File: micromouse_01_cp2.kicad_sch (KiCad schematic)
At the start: 40 parts, among them IC1 ESP32-S3FH4R2, IC2 MPU-6500, IC3 AS5047P-ATSM, IC4 AS5047P-ATSM, IC5 DRV8835DSSR, J2 USB_B_Micro, M1 MK06-4.5, M2 MK06-4.5, SW2 SW_Push, U7 RTV-104DF333-S-40.000-TR

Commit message: [fix]アンテナ除去
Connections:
- net GND: now also J2.6 (Shield)
- no-connect marks 46 -> 45
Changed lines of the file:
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@@
   (no_connect (at 35.56 40.64))
   (no_connect (at 71.12 106.68))
-  (no_connect (at 38.1 81.28))
   (no_connect (at 104.14 43.18))
   (no_connect (at 134.62 43.18))
@@
     (stroke (width 0) (type default))
   )
+  (wire (pts (xy 38.1 88.9) (xy 40.64 88.9))
+    (stroke (width 0) (type default))
+  )
   (wire (pts (xy 100.33 30.48) (xy 104.14 30.48))
     (stroke (width 0) (type default))
@@
     (stroke (width 0) (type default))
   )
+  (wire (pts (xy 38.1 81.28) (xy 38.1 88.9))
+    (stroke (width 0) (type default))
+  )

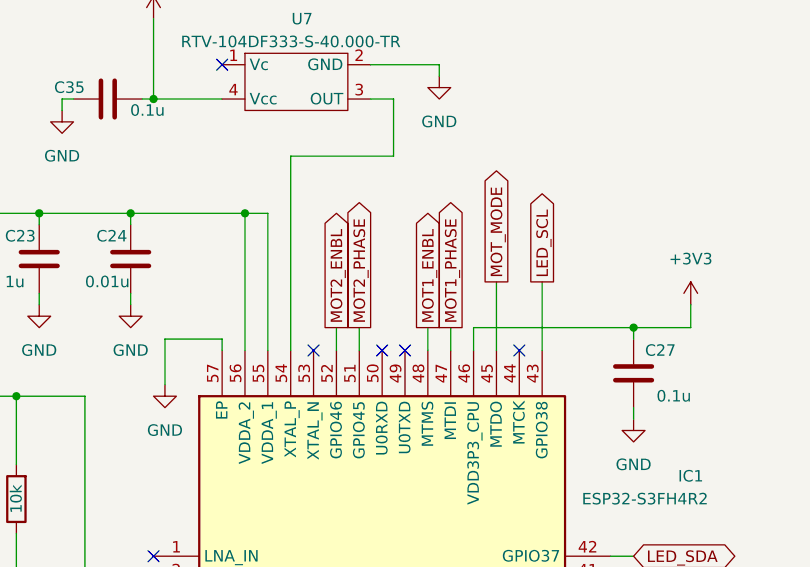
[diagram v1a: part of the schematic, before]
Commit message: [add]LED追加
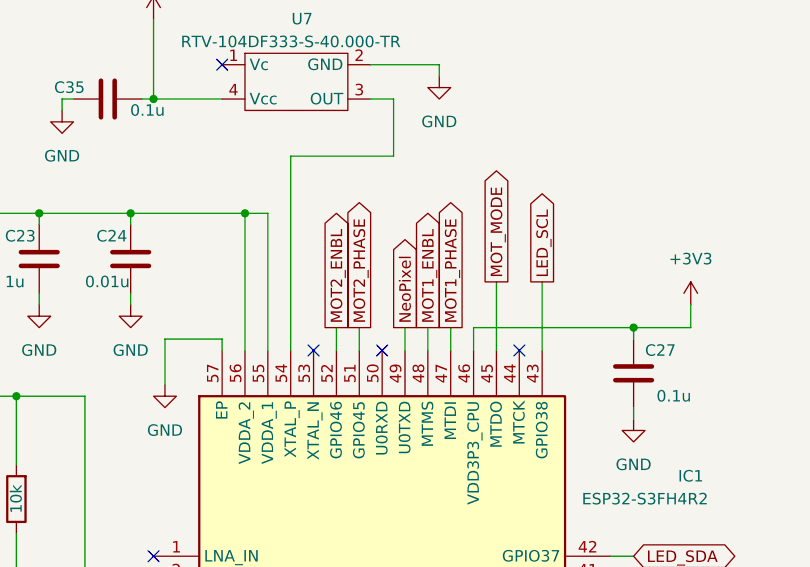
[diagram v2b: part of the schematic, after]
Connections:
- net NeoPixel: now reaches IC1.49 (U0TXD)
- no-connect marks 45 -> 44
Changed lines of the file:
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@@
   (no_connect (at 246.38 114.3))
   (no_connect (at 246.38 99.06))
-  (no_connect (at 220.98 60.96))
   (no_connect (at 96.52 116.84))
   (no_connect (at 203.2 29.21))
@@
   (no_connect (at 236.22 139.7))
   (no_connect (at 68.58 106.68))
-  (no_connect (at 223.52 60.96))
+  (no_connect (at 220.98 60.96))
   (no_connect (at 60.96 137.16))
   (no_connect (at 134.62 27.94))
@@
     (stroke (width 0) (type default))
   )
+  (wire (pts (xy 223.52 58.42) (xy 223.52 60.96))
+    (stroke (width 0) (type default))
+  )
   (wire (pts (xy 125.73 177.8) (xy 128.27 177.8))
     (stroke (width 0) (type default))
@@
       (effects (font (size 1.27 1.27)) (justify left) hide)
     )
+  )
+  (global_label "NeoPixel" (shape output) (at 223.52 58.42 90) (fields_autoplaced)
+    (effects (font (size 1.27 1.27)) (justify left))
+    (property "Intersheetrefs" "${INTERSHEET_REFS}" (at 223.52 47.21 90)
+      (effects (font (size 1.27 1.27)) (justify left) hide)
+    )

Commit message: 仮変更
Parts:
- removed C18, C25, C26, C27, C28, C29, C30, C31, C32, C35: 0.1u, Capacitor_SMD:C_0402_1005Metric, symbol Device:C
- removed C19, C20, C22, C23: 1u, Capacitor_SMD:C_0402_1005Metric, symbol Device:C
- removed C21: 10u, Capacitor_SMD:C_0603_1608Metric, symbol Device:C
- removed C24: 0.01u, Capacitor_SMD:C_0402_1005Metric, symbol Device:C
- removed D4, D5: ESD9B3.3ST5G, Diode_SMD:D_SOD-923, symbol Diode:ESD9B3.3ST5G
- removed IC1: ESP32-S3FH4R2, footprints:QFN40P700X700X90-57N-D, symbol ESP32-S3FH4R2:ESP32-S3FH4R2
- removed J2: USB_B_Micro, footprints:WURTH_614105150721, symbol Connector:USB_B_Micro
- removed L1: 2.0nH, Inductor_SMD:L_0402_1005Metric, symbol Device:L
- removed R24: 10k, Resistor_SMD:R_0402_1005Metric, symbol Device:R
- removed SW2: SW_Push, footprints:BOOT_PAD, symbol Switch:SW_Push
- removed U7: RTV-104DF333-S-40.000-TR, Crystal:Crystal_SMD_2016-4Pin_2.0x1.6mm, symbol RTV-104DF333-S-40.000-TR:RTV-104DF333-S-40.000-TR
- added C33, C34, C36, C38, C9: 0.1u, Capacitor_SMD:C_0402_1005Metric, symbol Device:C
- added C37: 22u, Capacitor_SMD:C_0603_1608Metric, symbol Device:C
- added C41: 1u, Capacitor_SMD:C_0402_1005Metric, symbol Device:C
- added J3: ~, footprints:ZX62R-B-5P_30_, symbol ZX62R_B_5P_30_:ZX62R_B_5P_30_
- added R21: 10k, Resistor_SMD:R_0402_1005Metric, symbol Device:R
- added R32, R33: 20, Resistor_SMD:R_0402_1005Metric, symbol Device:R
- added U9: ESP32-S3-PICO-1-N8R2, QFN56_7X7_EXP, symbol 2024-02-29_13-39-39:ESP32-S3-PICO-1-N8R2
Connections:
- net +3V3: now also C37.1, C38.1, R21.2, U9.2 (VDD3P3), U9.20 (VDD3P3_RTC), U9.3 (VDD3P3), U9.46 (VDD3P3_CPU), U9.55 (VDDA), U9.56 (VDDA)
- net BOOT: now also U9.5 (GPIO0)
- net BUZZER: now also U9.19 (GPIO14)
- net ENCL_CS: now also U9.11 (GPIO6)
- net ENCR_CS: now also U9.6 (GPIO1)
- net ENC_CLK: now also U9.39 (GPIO34)
- net ENC_MISO: now also U9.40 (GPIO35)
- net ENC_MOSI: now also U9.41 (GPIO36)
- net FAN_PWM: now also U9.18 (GPIO13)
- net GND: now also C33.2, C34.2, C36.2, C37.2, C38.2, C41.1, C9.2, J3.10, J3.11, J3.5 (GND), J3.6 (Shield), J3.7, J3.8, J3.9, U9.57 (GND)
- net IMU_CLK: now also U9.7 (GPIO2)
- net IMU_CS: now also U9.12 (GPIO7)
- net IMU_MISO: now also U9.16 (GPIO11)
- net IMU_MOSI: now also U9.17 (GPIO12)
- net LED_FL: now also U9.23 (GPIO17)
- net LED_FR: now also U9.38 (GPIO33)
- net LED_L: now also U9.24 (GPIO18)
- net LED_R: now also U9.27 (GPIO21)
- net LED_SCL: now also U9.43 (GPIO38)
- net LED_SDA: now also U9.42 (GPIO37)
- net MOT1_ENBL: now also U9.48 (MTMS)
- net MOT1_PHASE: now also U9.47 (MTDI)
- net MOT2_ENBL: now also U9.52 (GPIO46)
- net MOT2_PHASE: now also U9.51 (GPIO45)
- net MOT_MODE: now also U9.45 (MTDO)
- net NeoPixel: now also U9.21 (XTAL_32K_P)
- net SENS_FL: now also C36.1, U9.15 (GPIO10)
- net SENS_FR: now also C9.1, U9.9 (GPIO4)
- net SENS_L: now also C34.1, U9.13 (GPIO8)
- net SENS_R: now also C33.1, U9.10 (GPIO5)
- net USB_D+: now also R33.2, U9.26 (GPIO20)
- net USB_D-: now also R32.2, U9.25 (GPIO19)
- net VBATT: now also U9.8 (GPIO3)
- net VBUS: now reaches C14.1
- net VBUS: now also J3.1 (VBUS)
- new net: J3.2 (D-), R32.1
- new net: J3.3 (D+), R33.1
- new net CHIP_PU: C41.2, R21.1, U9.4 (CHIP_PU)
- no-connect marks 44 -> 45
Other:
- moved on the sheet: C14, R3

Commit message: [update]けっこう線引いた
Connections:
- net ENC_CLK: now also U9.41 (GPIO36); no longer U9.39 (GPIO34)
- net ENC_MOSI: now also U9.39 (GPIO34); no longer U9.41 (GPIO36)
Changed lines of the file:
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@@
+    )
+  )
+  (global_label "ENC_MOSI" (shape output) (at 256.54 101.6 0) (fields_autoplaced)
+    (effects (font (size 1.27 1.27)) (justify left))
+    (property "Intersheetrefs" "${INTERSHEET_REFS}" (at 268.8385 101.6 0)
+      (effects (font (size 1.27 1.27)) (justify left) hide)
     )
   )
@@
     )
   )
+  (global_label "ENC_CLK" (shape output) (at 256.54 96.52 0) (fields_autoplaced)
+    (effects (font (size 1.27 1.27)) (justify left))
+    (property "Intersheetrefs" "${INTERSHEET_REFS}" (at 267.8104 96.52 0)
+      (effects (font (size 1.27 1.27)) (justify left) hide)
+    )
+  )
   (global_label "ENC_MISO" (shape output) (at 100.33 33.02 180) (fields_autoplaced)
     (effects (font (size 1.27 1.27)) (justify right))
@@
     )
   )
-  (global_label "ENC_CLK" (shape output) (at 256.54 101.6 0) (fields_autoplaced)
-    (effects (font (size 1.27 1.27)) (justify left))
-    (property "Intersheetrefs" "${INTERSHEET_REFS}" (at 267.8104 101.6 0)
-      (effects (font (size 1.27 1.27)) (justify left) hide)
-    )
-  )
   (global_label "IMU_MOSI" (shape input) (at 31.75 127 180) (fields_autoplaced)
     (effects (font (size 1.27 1.27)) (justify right))
     (property "Intersheetrefs" "${INTERSHEET_REFS}" (at 19.8143 127 0)
       (effects (font (size 1.27 1.27)) (justify right) hide)
-    )
-  )
-  (global_label "ENC_MOSI" (shape output) (at 256.54 96.52 0) (fields_autoplaced)
-    (effects (font (size 1.27 1.27)) (justify left))
-    (property "Intersheetrefs" "${INTERSHEET_REFS}" (at 268.8385 96.52 0)
-      (effects (font (size 1.27 1.27)) (justify left) hide)
     )
   )
@@
     )
   )
-  (symbol (lib_id "Device:C") (at 187.96 27.94 0) (unit 1)
+  (symbol (lib_id "Device:C") (at 187.96 27.94 0) (mirror y) (unit 1)
     (in_bom yes) (on_board yes) (dnp no)
-    (property "Reference" "C38" (at 189.23 25.4 0)
-      (effects (font (size 1.27 1.27)) (justify left))
-    )
-    (property "Value" "0.1u" (at 189.23 30.48 0)
-      (effects (font (size 1.27 1.27)) (justify left))
-    )
-    (property "Footprint" "Capacitor_SMD:C_0402_1005Metric" (at 188.9252 31.75 0)
-      (effects (font (size 1.27 1.27)) hide)
-    )
+    (property "Reference" "C38" (at 186.69 25.4 0)
+      (effects (font (size 1.27 1.27)) (justify left))
+    )
+    (property "Value" "0.1u" (at 186.69 30.48 0)
+      (effects (font (size 1.27 1.27)) (justify left))
+    )
+    (property "Footprint" "Capacitor_SMD:C_0402_1005Metric" (at 186.9948 31.75 0)
+      (effects (font (size 1.27 1.27)) hide)
+    )

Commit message: エンコーダ基板変更前コミット
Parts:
- added C12, C20: 1u, Capacitor_SMD:C_0402_1005Metric, symbol Device:C
- added U10, U11: MA730, Package_DFN_QFN:QFN-16-1EP_3x3mm_P0.5mm_EP1.75x1.75mm, symbol Sensor_Magnetic:MA730
- added U12: MCP3464T-E/NC, UQFN20_NC_MCH, symbol 2024-03-13_05-36-02:MCP3464T-E_NC
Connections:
- net +3V3: now also C12.1, C20.1, U10.13 (VDD), U11.13 (VDD)
- net ENCL_CS: now also U10.5 (~{CS})
- net ENCR_CS: now also U11.5 (~{CS})
- net ENC_CLK: now also U10.12 (SCLK), U11.12 (SCLK)
- net ENC_MISO: now also U10.7 (MISO), U11.7 (MISO)
- net ENC_MOSI: now also U10.4 (MOSI), U11.4 (MOSI)
- net GND: now also C12.2, C20.2, U10.10 (TEST), U10.17 (PAD), U10.8 (GND), U11.10 (TEST), U11.17 (PAD), U11.8 (GND)
- no-connect marks 45 -> 61

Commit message: とりあえず回路図完成
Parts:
- removed C33, C34, C36, C9: 0.1u, Capacitor_SMD:C_0402_1005Metric, symbol Device:C
- removed IC3, IC4: AS5047P-ATSM, footprints:SOP65P640X120-14N, symbol AS5047P-ATSM:AS5047P-ATSM
- removed U12: MCP3464T-E/NC, UQFN20_NC_MCH, symbol 2024-03-13_05-36-02:MCP3464T-E_NC
- added C21, C22, C23, C24: 0.1u, Capacitor_SMD:C_0402_1005Metric, symbol Device:C
- added R20: 0, symbol Device:R
- added U13: MCP3464T-E/NC, UQFN20_NC_MCH, symbol 2024-03-13_05-36-02:MCP3464T-E_NC
- C6, C7: footprint Capacitor_SMD:C_0402_1005Metric -> (none)
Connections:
- net +3V3: now also R20.1, U13.18 (DVDD), U13.19 (AVDD)
- net GND: now also C21.2, C22.2, C23.2, C24.2, U13.1 (REFIN-), U13.17 (DGND), U13.20 (AGND), U13.21 (AGND)
- net IMU_CLK: now also U13.12 (SCK)
- net IMU_MISO: now also U13.14 (SDO)
- net IMU_MOSI: now also U13.13 (SDI)
- net SENS_FL: now also C24.1, U13.6 (CH3); no longer U9.15 (GPIO10)
- net SENS_FR: now also C21.1, U13.3 (CH0); no longer U9.9 (GPIO4)
- net SENS_L: now also C23.1, U13.5 (CH2); no longer U9.13 (GPIO8)
- net SENS_R: now also C22.1, U13.4 (CH1); no longer U9.10 (GPIO5)
- net VBATT: now also U13.7 (CH4); no longer U9.8 (GPIO3)
- new net: R20.2, U13.2 (REFIN+)
- new net ADC_CS: U13.11 (CS), U9.9 (GPIO4)
- no-connect marks 61 -> 54
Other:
- moved on the sheet: C12, C20, C37, C38, C41, R21, R3, U10, U11, U9

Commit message: パターン配線中
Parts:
- added AE1: Antenna_Shield, RF_Antenna:Texas_SWRA117D_2.4GHz_Right, symbol Device:Antenna_Shield
- added C25, C9: 3.3p, Capacitor_SMD:C_0402_1005Metric, symbol Device:C
- added L1: 2.2n, Inductor_SMD:L_0402_1005Metric, symbol Device:L
- C6, C7: footprint (none) -> Capacitor_SMD:C_0402_1005Metric
- R20: footprint (none) -> Resistor_SMD:R_0402_1005Metric
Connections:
- net ADC_CS: now also U9.10 (GPIO5); no longer U9.9 (GPIO4)
- net BUZZER: now also U9.18 (GPIO13); no longer U9.19 (GPIO14)
- net ENCL_CS: now also U9.13 (GPIO8); no longer U9.11 (GPIO6)
- net FAN_PWM: now also U9.16 (GPIO11); no longer U9.18 (GPIO13)
- net GND: now also AE1.2 (Shield), C25.2, C9.2
- net IMU_CLK: now also U9.9 (GPIO4); no longer U9.7 (GPIO2)
- net IMU_CS: now also U9.19 (GPIO14); no longer U9.12 (GPIO7)
- net IMU_MISO: now also U9.7 (GPIO2); no longer U9.16 (GPIO11)
- net IMU_MOSI: now also U9.8 (GPIO3); no longer U9.17 (GPIO12)
- net LED_L: now also U9.15 (GPIO10); no longer U9.24 (GPIO18)
- net LED_SCL: now also U9.42 (GPIO37); no longer U9.43 (GPIO38)
- net LED_SDA: now also U9.43 (GPIO38); no longer U9.42 (GPIO37)
- net SENS_FL: now also C23.1, U13.5 (CH2); no longer C24.1, U13.6 (CH3)
- net SENS_L: now also C24.1, U13.6 (CH3); no longer C23.1, U13.5 (CH2)
- net at U9.1 (LNA_IN): now also C25.1, L1.2
- new net: AE1.1 (A), C9.1, L1.1
- no-connect marks 54 -> 57

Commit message: [update]いい感じ
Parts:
- R32, R33: value 20 -> 22
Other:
- moved on the sheet: C14, R32, R33
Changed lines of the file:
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@@
   (junction (at 243.84 129.54) (diameter 0) (color 0 0 0 0)
   )
-  (junction (at 91.44 66.04) (diameter 0) (color 0 0 0 0)
+  (junction (at 80.01 66.04) (diameter 0) (color 0 0 0 0)
   )
   (junction (at 175.26 17.78) (diameter 0) (color 0 0 0 0)
@@
     (stroke (width 0) (type default))
   )
-  (wire (pts (xy 67.31 71.12) (xy 104.14 71.12))
+  (wire (pts (xy 57.15 71.12) (xy 60.96 71.12))
     (stroke (width 0) (type default))
   )
@@
     (stroke (width 0) (type default))
   )
-  (wire (pts (xy 48.26 66.04) (xy 91.44 66.04))
+  (wire (pts (xy 48.26 66.04) (xy 80.01 66.04))
     (stroke (width 0) (type default))
   )
@@
     (stroke (width 0) (type default))
   )
-  (wire (pts (xy 74.93 73.66) (xy 104.14 73.66))
+  (wire (pts (xy 57.15 73.66) (xy 60.96 73.66))
     (stroke (width 0) (type default))
   )
@@
     (stroke (width 0) (type default))
   )
-  (wire (pts (xy 48.26 71.12) (xy 59.69 71.12))
+  (wire (pts (xy 48.26 71.12) (xy 49.53 71.12))
     (stroke (width 0) (type default))
   )
@@
     (stroke (width 0) (type default))
   )
-  (wire (pts (xy 40.64 88.9) (xy 91.44 88.9))
+  (wire (pts (xy 40.64 88.9) (xy 80.01 88.9))
     (stroke (width 0) (type default))
   )
@@
     (stroke (width 0) (type default))
   )
-  (wire (pts (xy 91.44 66.04) (xy 91.44 63.5))
+  (wire (pts (xy 80.01 66.04) (xy 80.01 63.5))
     (stroke (width 0) (type default))
   )
@@
     (stroke (width 0) (type default))
   )
-  (wire (pts (xy 91.44 85.09) (xy 91.44 88.9))
+  (wire (pts (xy 80.01 85.09) (xy 80.01 88.9))
     (stroke (width 0) (type default))
   )
@@
     (stroke (width 0) (type default))
   )
-  (wire (pts (xy 48.26 73.66) (xy 67.31 73.66))
+  (wire (pts (xy 48.26 73.66) (xy 49.53 73.66))
     (stroke (width 0) (type default))
   )
@@
     (stroke (width 0) (type default))
   )
-  (wire (pts (xy 91.44 77.47) (xy 91.44 66.04))
+  (wire (pts (xy 80.01 77.47) (xy 80.01 66.04))
     (stroke (width 0) (type default))
   )
@@
     )
   )
-  (global_label "USB_D-" (shape bidirectional) (at 104.14 73.66 0) (fields_autoplaced)
+  (global_label "USB_D-" (shape bidirectional) (at 60.96 73.66 0) (fields_autoplaced)
     (effects (font (size 1.27 1.27)) (justify left))
-    (property "Intersheetrefs" "${INTERSHEET_REFS}" (at 115.8565 73.66 0)
+    (property "Intersheetrefs" "${INTERSHEET_REFS}" (at 72.6765 73.66 0)
       (effects (font (size 1.27 1.27)) (justify left) hide)
     )
@@
     )
   )
-  (global_label "USB_D+" (shape bidirectional) (at 104.14 71.12 0) (fields_autoplaced)
+  (global_label "USB_D+" (shape bidirectional) (at 60.96 71.12 0) (fields_autoplaced)
     (effects (font (size 1.27 1.27)) (justify left))
-    (property "Intersheetrefs" "${INTERSHEET_REFS}" (at 115.8565 71.12 0)
+    (property "Intersheetrefs" "${INTERSHEET_REFS}" (at 72.6765 71.12 0)
       (effects (font (size 1.27 1.27)) (justify left) hide)
     )
@@
     )
   )
-  (symbol (lib_id "Device:R") (at 71.12 73.66 90) (unit 1)
-    (in_bom yes) (on_board yes) (dnp no) (fields_autoplaced)
-    (property "Reference" "R32" (at 71.12 67.31 90)
-      (effects (font (size 1.27 1.27)))
-    )
-    (property "Value" "20" (at 71.12 69.85 90)
-      (effects (font (size 1.27 1.27)))
-    )
-    (property "Footprint" "Resistor_SMD:R_0402_1005Metric" (at 71.12 75.438 90)
-      (effects (font (size 1.27 1.27)) hide)
-    )
-    (property "Datasheet" "~" (at 71.12 73.66 0)
+  (symbol (lib_id "Device:R") (at 53.34 73.66 90) (unit 1)
+    (in_bom yes) (on_board yes) (dnp no)
+    (property "Reference" "R32" (at 53.34 76.2 90)
+      (effects (font (size 1.27 1.27)))
+    )
+    (property "Value" "22" (at 53.34 73.66 90)
+      (effects (font (size 1.27 1.27)))
+    )
+    (property "Footprint" "Resistor_SMD:R_0402_1005Metric" (at 53.34 75.438 90)
+      (effects (font (size 1.27 1.27)) hide)
+    )
+    (property "Datasheet" "~" (at 53.34 73.66 0)
       (effects (font (size 1.27 1.27)) hide)
     )
@@
     )
   )
-  (symbol (lib_id "Device:R") (at 63.5 71.12 90) (unit 1)
-    (in_bom yes) (on_board yes) (dnp no) (fields_autoplaced)
-    (property "Reference" "R33" (at 63.5 64.77 90)
-      (effects (font (size 1.27 1.27)))
-    )
-    (property "Value" "20" (at 63.5 67.31 90)
-      (effects (font (size 1.27 1.27)))
-    )
-    (property "Footprint" "Resistor_SMD:R_0402_1005Metric" (at 63.5 72.898 90)
-      (effects (font (size 1.27 1.27)) hide)
-    )
-    (property "Datasheet" "~" (at 63.5 71.12 0)
+  (symbol (lib_id "Device:R") (at 53.34 71.12 90) (unit 1)
+    (in_bom yes) (on_board yes) (dnp no)
+    (property "Reference" "R33" (at 53.34 68.58 90)
+      (effects (font (size 1.27 1.27)))
+    )
+    (property "Value" "22" (at 53.34 71.12 90)
+      (effects (font (size 1.27 1.27)))
+    )
+    (property "Footprint" "Resistor_SMD:R_0402_1005Metric" (at 53.34 72.898 90)
+      (effects (font (size 1.27 1.27)) hide)
+    )
+    (property "Datasheet" "~" (at 53.34 71.12 0)
       (effects (font (size 1.27 1.27)) hide)
     )
@@
     )
   )
-  (symbol (lib_id "Device:C") (at 91.44 81.28 0) (unit 1)
+  (symbol (lib_id "Device:C") (at 80.01 81.28 0) (unit 1)
     (in_bom yes) (on_board yes) (dnp no)
-    (property "Reference" "C14" (at 86.36 78.74 0)
-      (effects (font (size 1.27 1.27)) (justify left))
-    )
-    (property "Value" "0.1u" (at 86.36 83.82 0)
-      (effects (font (size 1.27 1.27)) (justify left))
-    )
-    (property "Footprint" "Capacitor_SMD:C_0402_1005Metric" (at 92.4052 85.09 0)
-      (effects (font (size 1.27 1.27)) hide)
-    )
-    (property "Datasheet" "~" (at 91.44 81.28 0)
+    (property "Reference" "C14" (at 74.93 78.74 0)
+      (effects (font (size 1.27 1.27)) (justify left))
+    )
+    (property "Value" "0.1u" (at 74.93 83.82 0)
+      (effects (font (size 1.27 1.27)) (justify left))
+    )
+    (property "Footprint" "Capacitor_SMD:C_0402_1005Metric" (at 80.9752 85.09 0)
+      (effects (font (size 1.27 1.27)) hide)
+    )
+    (property "Datasheet" "~" (at 80.01 81.28 0)
       (effects (font (size 1.27 1.27)) hide)
     )
@@
     )
   )
-  (symbol (lib_id "power:VBUS") (at 91.44 63.5 0) (unit 1)
-    (in_bom yes) (on_board yes) (dnp no) (fields_autoplaced)
-    (property "Reference" "#PWR018" (at 91.44 67.31 0)
-      (effects (font (size 1.27 1.27)) hide)
-    )
-    (property "Value" "VBUS" (at 91.44 58.42 0)
-      (effects (font (size 1.27 1.27)))
-    )
-    (property "Footprint" "" (at 91.44 63.5 0)
-      (effects (font (size 1.27 1.27)) hide)
-    )
-    (property "Datasheet" "" (at 91.44 63.5 0)
-      (effects (font (size 1.27 1.27)) hide)
-    )
+  (symbol (lib_id "power:VBUS") (at 80.01 63.5 0) (unit 1)
+    (in_bom yes) (on_board yes) (dnp no) (fields_autoplaced)
+    (property "Reference" "#PWR018" (at 80.01 67.31 0)
+      (effects (font (size 1.27 1.27)) hide)
+    )
+    (property "Value" "VBUS" (at 80.01 58.42 0)
+      (effects (font (size 1.27 1.27)))
+    )
+    (property "Footprint" "" (at 80.01 63.5 0)
+      (effects (font (size 1.27 1.27)) hide)
+    )
+    (property "Datasheet" "" (at 80.01 63.5 0)
+      (effects (font (size 1.27 1.27)) hide)
+    )
